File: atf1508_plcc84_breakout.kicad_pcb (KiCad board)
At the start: 2 copper layers, 140.8 x 32.6 mm, 13 parts, among them J1 Atmel-JTAG-10, J2 Conn_01x34, J3 Conn_01x34, U1 ATF1508AS-xJx84

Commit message: Update
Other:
- board size 140.8 x 32.6 mm -> 140.8 x 33 mm

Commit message: Update
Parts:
- added C10: 100n, Capacitor_SMD:C_0805_2012Metric_Pad1.18x1.45mm_HandSolder, B.Cu at (186.7, 61.7)
- added X1: xMHz, Oscillator:Oscillator_SMD_IQD_IQXO70-4Pin_7.5x5.0mm_HandSoldering, F.Cu at (186.6, 61.8)
- J2, J3: value Conn_01x34 -> Conn_01x35
- locked: footprint Capacitor_SMD:C_0805_2012Metric_Pad1.18x1.45mm_HandSolder -> Capacitor_THT:CP_Radial_D4.0mm_P1.50mm; moved to F.Cu
- moved locked 16.9 mm to (126.5, 62.2)
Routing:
- net VCC: track 145.5 -> 219.7 mm, vias 8 -> 10
- net /I/GCLK1: track 34.2 -> 93.8 mm, vias 1 -> 3
- net /B20: track 130.8 -> 137.3 mm
- net GND: track 285.6 -> 289.6 mm, vias 5 -> 6
- net /B22: track 130.4 -> 133.4 mm
- net /B21: track 129.2 -> 132.1 mm
- net /A8: track 102.4 -> 101.1 mm
- net /C31: track 107.3 -> 108.5 mm
- net /D33: track 108.4 -> 109.6 mm
- net /B15: track 120.2 -> 121.4 mm
- net /G63: track 66.8 -> 68.0 mm
- net /A12/PD1: track 121.0 -> 122.2 mm
- net /D34: track 103.1 -> 104.2 mm
- net /G65: track 62.4 -> 63.5 mm
- net /C27: track 117.5 -> 118.6 mm
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
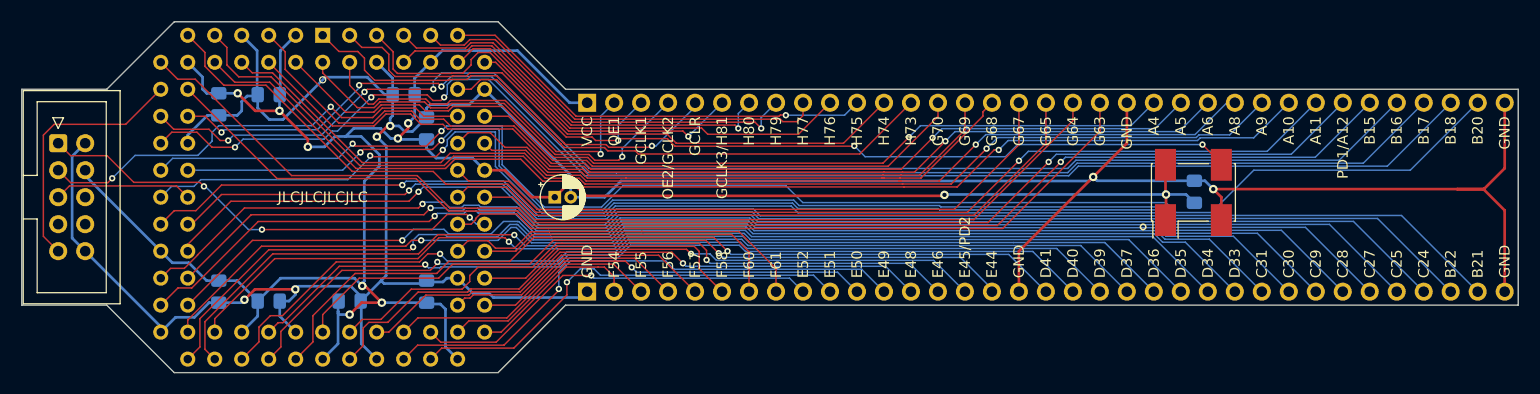
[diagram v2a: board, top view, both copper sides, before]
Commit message: Revert oscillator addition
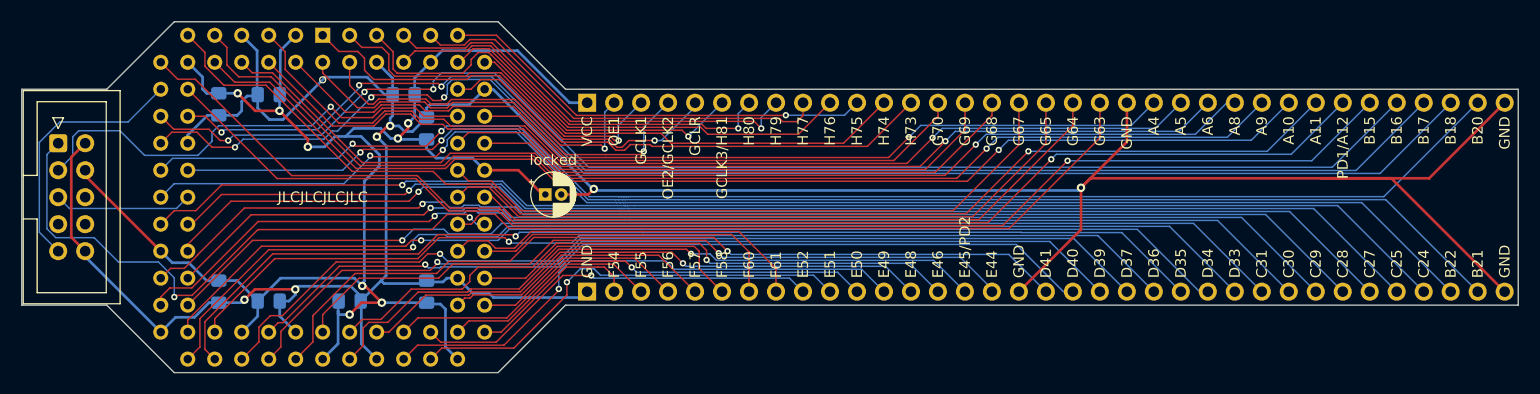
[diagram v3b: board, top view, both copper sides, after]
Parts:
- removed C10: 100n, Capacitor_SMD:C_0805_2012Metric_Pad1.18x1.45mm_HandSolder
- removed X1: xMHz, Oscillator:Oscillator_SMD_IQD_IQXO70-4Pin_7.5x5.0mm_HandSoldering
- moved locked 0.92 mm to (125.6, 62.0)
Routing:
- net VCC: track 219.7 -> 151.8 mm, vias 10 -> 8
- net /I/GCLK1: track 93.8 -> 35.0 mm, vias 3 -> 1
- net /JTAG_TCK: track 44.5 -> 57.0 mm, vias 3 -> 2
- net /B20: track 137.3 -> 132.3 mm
- net /B21: track 132.1 -> 129.4 mm
- net /B22: track 133.4 -> 130.7 mm
- net GND: track 289.6 -> 292.2 mm
- net /JTAG_TDO: track 42.6 -> 44.6 mm, vias 2 -> 1
- net /D34: track 104.2 -> 102.3 mm
- net /D33: track 109.6 -> 108.4 mm
- net /C31: track 108.5 -> 107.3 mm
- net /C29: track 113.3 -> 112.3 mm
- net /C27: track 118.6 -> 117.6 mm
- net /C28: track 118.9 -> 117.9 mm
- net /C24: track 125.6 -> 124.8 mm
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
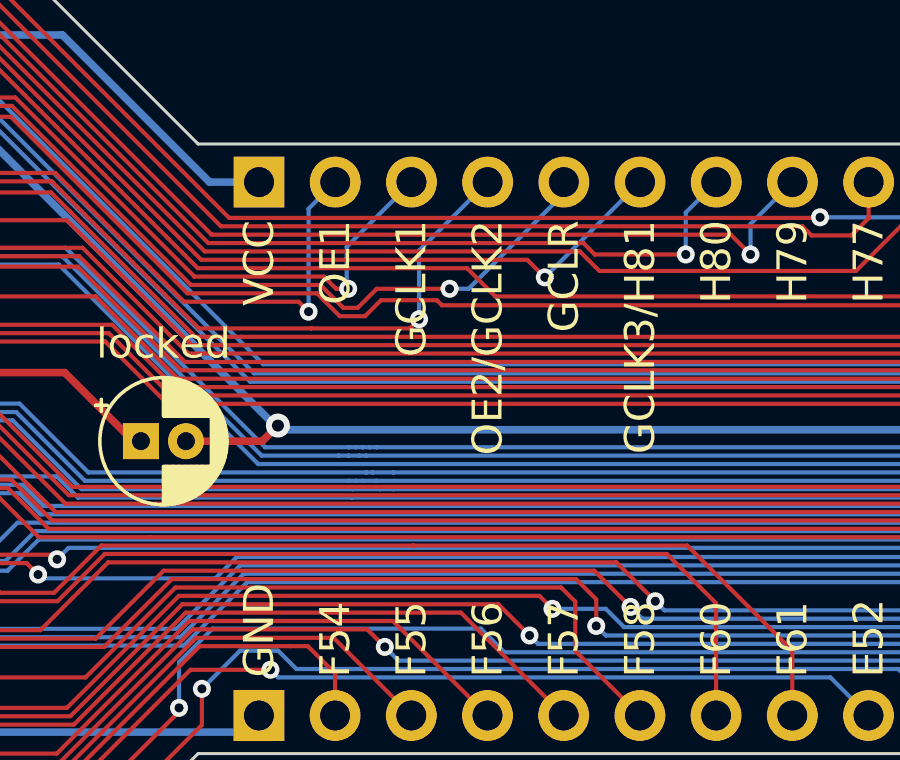
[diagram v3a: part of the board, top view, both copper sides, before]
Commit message: Add pin numbers for global inputs and re-order them
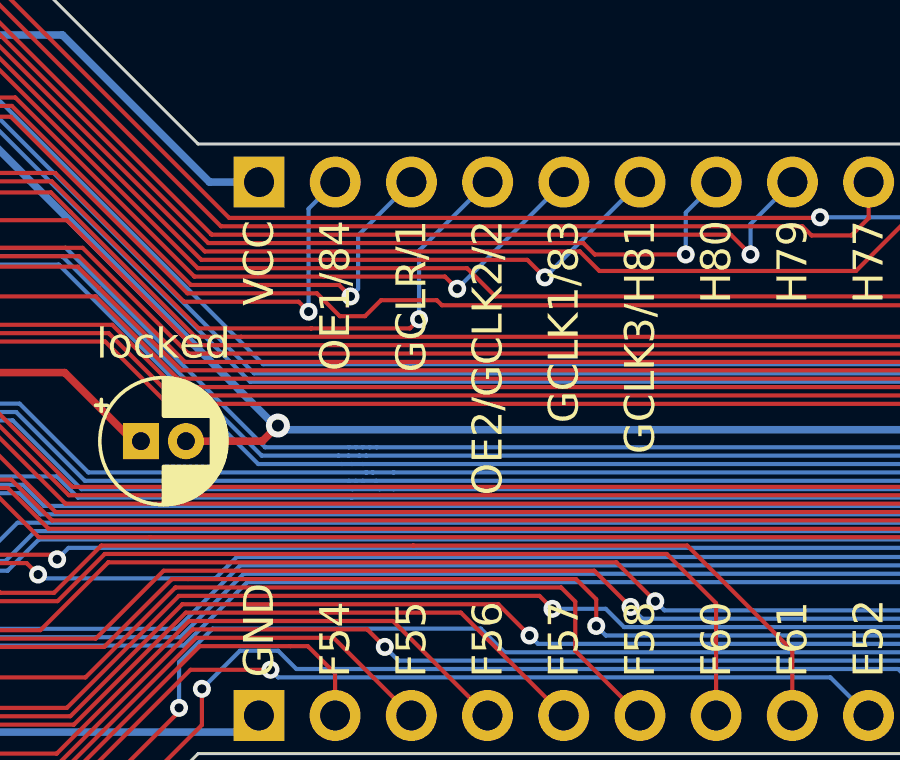
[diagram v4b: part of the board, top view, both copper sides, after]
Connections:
- J3 pad 3: /I/GCLK1 -> /I/GCLR
- J3 pad 5: /I/GCLR -> /I/GCLK1
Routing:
- net /I/GCLK1: track 35.0 -> 39.2 mm
- net /I/GCLR: track 41.9 -> 37.8 mm
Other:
- board text added: "ATF1508 Breakout 2023-07-15 - Rev B Adrien Kohlbecker"
- board text added: "GCLK1/83"
- board text added: "GCLR/1"
- board text added: "OE1/84"
- board text added: "OE2/GCLK2/2"
- board text removed: "ATF1508 Breakout 2023-06-17 - Rev A Adrien Kohlbecker"
- board text removed: "GCLK1"
- board text removed: "GCLR"
- board text removed: "OE1"
- board text removed: "OE2/GCLK2"
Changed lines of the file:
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@@
   (title_block
     (title "ATF1508 PLCC84 Breakout")
-    (date "2023-06-17")
-    (rev "A")
+    (date "2023-07-15")
+    (rev "B")
     (comment 2 "https://github.com/adrienkohlbecker/atf1508_plcc84_breakout")
     (comment 3 "Licensed under CERN-OHL-W v2")
@@
       (net 10 "/I{slash}OE1") (pinfunction "Pin_2") (pintype "passive"))
     (pad "3" thru_hole oval (at 0 -5.08 270) (size 1.7 1.7) (drill 1) (layers "*.Cu" "*.Mask")
-      (net 11 "/I{slash}GCLK1") (pinfunction "Pin_3") (pintype "passive"))
+      (net 23 "/I{slash}GCLR") (pinfunction "Pin_3") (pintype "passive"))
     (pad "4" thru_hole oval (at 0 -7.62 270) (size 1.7 1.7) (drill 1) (layers "*.Cu" "*.Mask")
       (net 24 "/I{slash}OE2{slash}GCLK2") (pinfunction "Pin_4") (pintype "passive"))
     (pad "5" thru_hole oval (at 0 -10.16 270) (size 1.7 1.7) (drill 1) (layers "*.Cu" "*.Mask")
-      (net 23 "/I{slash}GCLR") (pinfunction "Pin_5") (pintype "passive"))
+      (net 11 "/I{slash}GCLK1") (pinfunction "Pin_5") (pintype "passive"))
     (pad "6" thru_hole oval (at 0 -12.7 270) (size 1.7 1.7) (drill 1) (layers "*.Cu" "*.Mask")
       (net 46 "/H81{slash}GCLK3") (pinfunction "Pin_6") (pintype "passive"))
@@
   (gr_line (start 84.328 72.39) (end 76.327 72.39)
     (stroke (width 0.1) (type solid)) (layer "Edge.Cuts"))
-  (gr_text "ATF1508 Breakout\n2023-06-17 - Rev A\nAdrien Kohlbecker" (at 213.36 61.976) (layer "B.SilkS")
+  (gr_text "ATF1508 Breakout\n2023-07-15 - Rev B\nAdrien Kohlbecker" (at 213.36 61.976) (layer "B.SilkS")
     (effects (font (size 1 1) (thickness 0.15)) (justify left mirror))
   )
@@
     (effects (font (size 1 1) (thickness 0.15)) (justify left))
   )
-  (gr_text "OE1" (at 132.08 54.61 90) (layer "F.SilkS")
+  (gr_text "OE1/84" (at 132.08 54.61 90) (layer "F.SilkS")
     (effects (font (size 1 1) (thickness 0.15)) (justify right))
   )
@@
     (effects (font (size 1 1) (thickness 0.15)) (justify left))
   )
-  (gr_text "GCLR" (at 139.7 54.61 90) (layer "F.SilkS")
+  (gr_text "GCLR/1" (at 134.62 54.61 90) (layer "F.SilkS")
     (effects (font (size 1 1) (thickness 0.15)) (justify right))
   )
@@
     (effects (font (size 1 1) (thickness 0.15)) (justify right))
   )
-  (gr_text "OE2/GCLK2" (at 137.16 54.61 90) (layer "F.SilkS")
+  (gr_text "OE2/GCLK2/2" (at 137.16 54.61 90) (layer "F.SilkS")
     (effects (font (size 1 1) (thickness 0.15)) (justify right))
   )
@@
     (effects (font (size 1 1) (thickness 0.15)) (justify right))
   )
-  (gr_text "GCLK1" (at 134.62 54.61 90) (layer "F.SilkS")
+  (gr_text "GCLK1/83" (at 139.7 54.61 90) (layer "F.SilkS")
     (effects (font (size 1 1) (thickness 0.15)) (justify right))
   )
@@
   (segment (start 107.188 46.99) (end 108.331 48.133) (width 0.1397) (layer "F.Cu") (net 11))
   (segment (start 110.871 50.292) (end 111.42345 50.84445) (width 0.1397) (layer "F.Cu") (net 11))
-  (segment (start 131.701865 56.4896) (end 132.108264 56.896) (width 0.1397) (layer "F.Cu") (net 11))
+  (segment (start 131.701865 56.4896) (end 135.7376 56.4896) (width 0.1397) (layer "F.Cu") (net 11))
+  (segment (start 135.7376 56.4896) (end 136.144 56.896) (width 0.1397) (layer "F.Cu") (net 11))
   (segment (start 118.16715 50.84445) (end 118.491001 50.5206) (width 0.1397) (layer "F.Cu") (net 11))
   (segment (start 110.871 48.768) (end 110.871 50.292) (width 0.1397) (layer "F.Cu") (net 11))
-  (segment (start 132.108264 56.896) (end 132.461 56.896) (width 0.1397) (layer "F.Cu") (net 11))
-  (via (at 132.5118 56.896) (size 0.6) (drill 0.3) (layers "F.Cu" "B.Cu") (net 11))
-  (segment (start 132.461 55.499) (end 132.461 56.896) (width 0.1397) (layer "B.Cu") (net 11))
-  (segment (start 134.62 53.34) (end 132.461 55.499) (width 0.1397) (layer "B.Cu") (net 11))
+  (via (at 136.144 56.896) (size 0.6) (drill 0.3) (layers "F.Cu" "B.Cu") (net 11))
+  (segment (start 136.144 56.896) (end 139.7 53.34) (width 0.1397) (layer "B.Cu") (net 11))
   (segment (start 106.210599 68.731901) (end 114.137152 68.731901) (width 0.1397) (layer "F.Cu") (net 12))
   (segment (start 100.457 74.041) (end 100.9015 74.041) (width 0.1397) (layer "F.Cu") (net 12))
@@
   (segment (start 112.50295 60.72505) (end 121.55805 60.72505) (width 0.1397) (layer "B.Cu") (net 22))
   (segment (start 112.141 61.087) (end 112.50295 60.72505) (width 0.1397) (layer "B.Cu") (net 22))
-  (segment (start 132.348132 57.531) (end 132.827869 57.531) (width 0.1397) (layer "F.Cu") (net 23))
   (segment (start 104.648 46.99) (end 106.172 48.514) (width 0.1397) (layer "F.Cu") (net 23))
   (segment (start 108.585 50.277101) (end 109.457148 51.14925) (width 0.1397) (layer "F.Cu") (net 23))
-  (segment (start 133.462869 56.896) (end 135.89 56.896) (width 0.1397) (layer "F.Cu") (net 23))
-  (segment (start 132.827869 57.531) (end 133.462869 56.896) (width 0.1397) (layer "F.Cu") (net 23))
   (segment (start 106.172 48.514) (end 107.95 48.514) (width 0.1397) (layer "F.Cu") (net 23))
-  (segment (start 131.586133 56.769) (end 132.348132 57.531) (width 0.1397) (layer "F.Cu") (net 23))
   (segment (start 118.606732 50.8) (end 121.298946 50.8) (width 0.1397) (layer "F.Cu") (net 23))
   (segment (start 108.585 49.149) (end 108.585 50.277101) (width 0.1397) (layer "F.Cu") (net 23))
   (segment (start 121.298946 50.8) (end 127.267948 56.769) (width 0.1397) (layer "F.Cu") (net 23))
+  (segment (start 132.207 56.769) (end 132.588 57.15) (width 0.1397) (layer "F.Cu") (net 23))
+  (segment (start 131.586133 56.769) (end 132.207 56.769) (width 0.1397) (layer "F.Cu") (net 23))
   (segment (start 107.95 48.514) (end 108.585 49.149) (width 0.1397) (layer "F.Cu") (net 23))
   (segment (start 127.267948 56.769) (end 131.586133 56.769) (width 0.1397) (layer "F.Cu") (net 23))
   (segment (start 109.457148 51.14925) (end 118.257482 51.14925) (width 0.1397) (layer "F.Cu") (net 23))
   (segment (start 118.257482 51.14925) (end 118.606732 50.8) (width 0.1397) (layer "F.Cu") (net 23))
-  (via (at 135.89 56.896) (size 0.6) (drill 0.3) (layers "F.Cu" "B.Cu") (net 23))
-  (segment (start 139.7 53.721) (end 136.525 56.896) (width 0.1397) (layer "B.Cu") (net 23))
-  (segment (start 136.525 56.896) (end 135.89 56.896) (width 0.1397) (layer "B.Cu") (net 23))
+  (via (at 132.588 57.15) (size 0.6) (drill 0.3) (layers "F.Cu" "B.Cu") (net 23))
+  (segment (start 132.842 56.896) (end 132.842 55.118) (width 0.1397) (layer "B.Cu") (net 23))
+  (segment (start 132.588 57.15) (end 132.842 56.896) (width 0.1397) (layer "B.Cu") (net 23))
+  (segment (start 132.842 55.118) (end 134.62 53.34) (width 0.1397) (layer "B.Cu") (net 23))
   (segment (start 114.238222 53.264796) (end 114.796026 53.8226) (width 0.1397) (layer "F.Cu") (net 24))
   (segment (start 104.648 50.535788) (end 107.91041 53.798198) (width 0.1397) (layer "F.Cu") (net 24))
